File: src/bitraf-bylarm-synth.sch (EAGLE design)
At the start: 26 parts, among them IC1 LM386M-1, IC2 40106

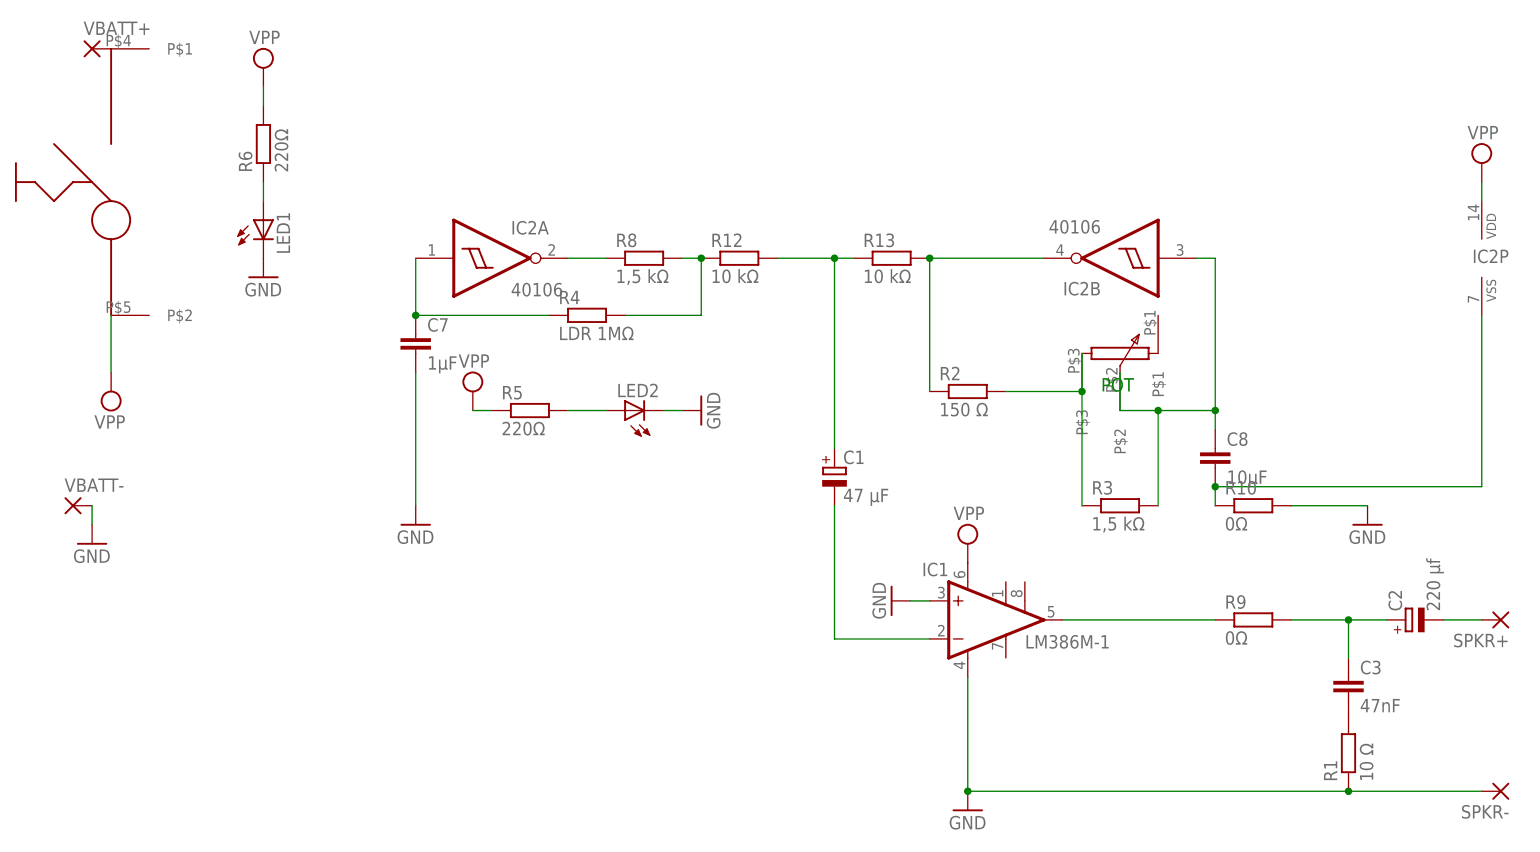
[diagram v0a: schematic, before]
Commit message: Tweak schematics and layout for actual values used
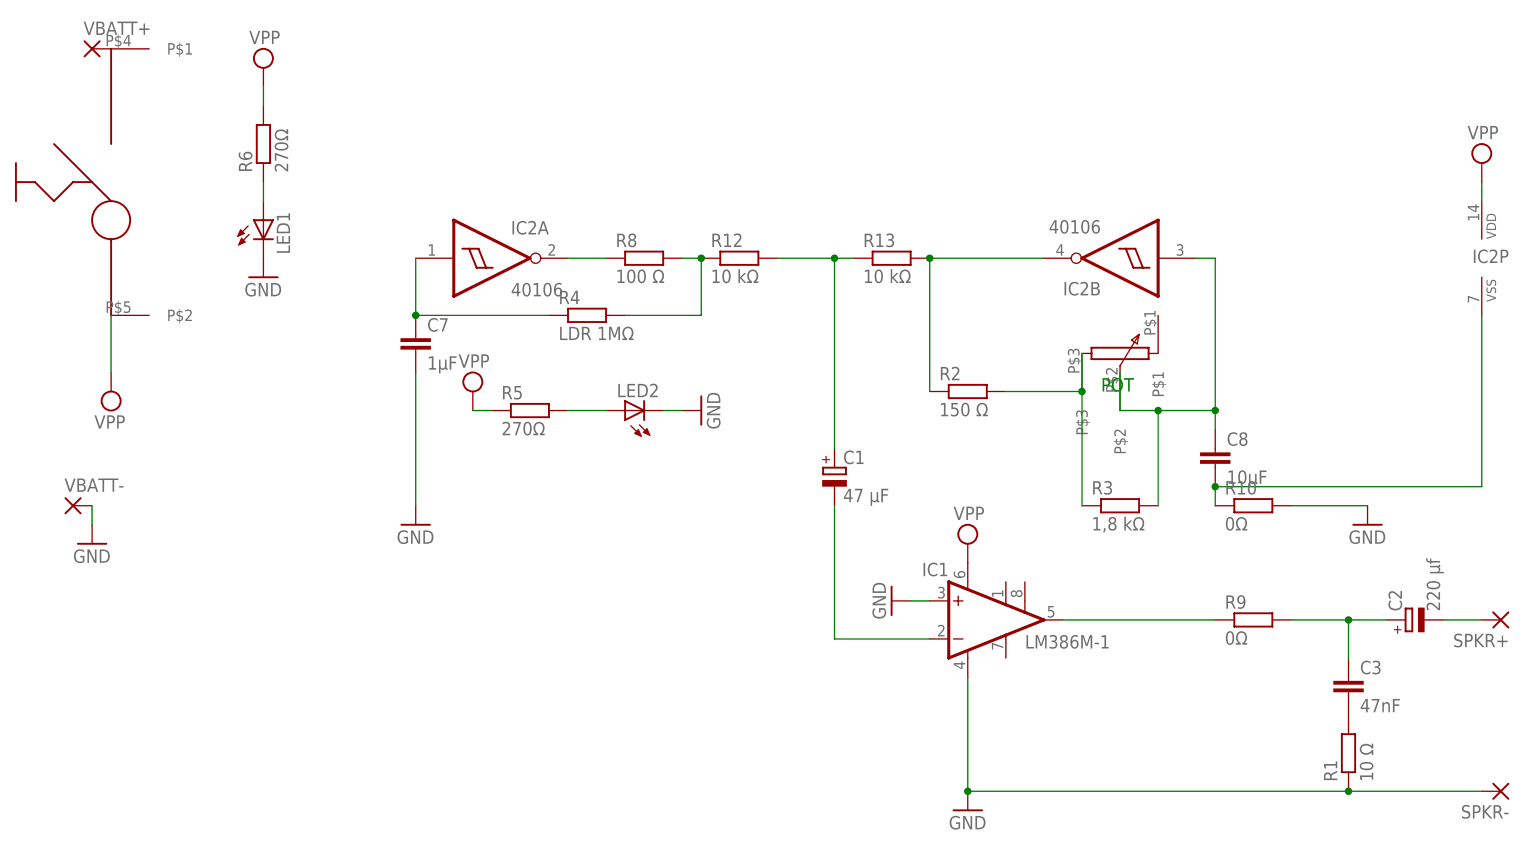
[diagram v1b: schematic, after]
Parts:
- R3: value 1,5 kΩ -> 1,8 kΩ
- R5, R6: value 220Ω -> 270Ω
- R8: value 1,5 kΩ -> 100 Ω
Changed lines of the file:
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@@
 <part name="C7" library="rcl" deviceset="C-EU" device="C0603" value="1µF"/>
 <part name="C8" library="rcl" deviceset="C-EU" device="C1206" value="10µF"/>
-<part name="R8" library="rcl" deviceset="R-EU_" device="R1206" value="1,5 kΩ"/>
+<part name="R8" library="rcl" deviceset="R-EU_" device="R1206" value="100 Ω"/>
 <part name="R12" library="rcl" deviceset="R-EU_" device="R1206" value="10 kΩ"/>
 <part name="R13" library="rcl" deviceset="R-EU_" device="R1206" value="10 kΩ"/>
@@
 <part name="C3" library="rcl" deviceset="C-EU" device="C0402" value="47nF"/>
 <part name="R2" library="rcl" deviceset="R-EU_" device="R1206" value="150 Ω"/>
-<part name="R3" library="rcl" deviceset="R-EU_" device="R1206" value="1,5 kΩ"/>
+<part name="R3" library="rcl" deviceset="R-EU_" device="R1206" value="1,8 kΩ"/>
 <part name="R4" library="rcl" deviceset="R-EU_" device="0204/2V" value="LDR 1MΩ"/>
 <part name="U$1" library="smallpot" deviceset="SMALLPOT" device=""/>
-<part name="R5" library="rcl" deviceset="R-EU_" device="R2512" value="220Ω"/>
-<part name="R6" library="rcl" deviceset="R-EU_" device="R2512" value="220Ω"/>
+<part name="R5" library="rcl" deviceset="R-EU_" device="R2512" value="270Ω"/>
+<part name="R6" library="rcl" deviceset="R-EU_" device="R2512" value="270Ω"/>
 <part name="SUPPLY3" library="supply2" deviceset="VPP" device=""/>
 <part name="SUPPLY4" library="supply2" deviceset="VPP" device=""/>
